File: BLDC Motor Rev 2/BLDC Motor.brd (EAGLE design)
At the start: 60.6 x 67 mm, 51 parts, among them IC1 7805TV, IC2 7815TV, Q1 TP2104, Q10 TP2104, Q12 IRFS, Q13 TP2104, Q15 IRFS, Q16 TP2104, Q18 IRFS, Q3 IRFS, Q4 TP2104, Q6 IRFS, Q7 TP2104, Q9 IRFS, U1 ATMEGA328P_TQFP, Y1 16M

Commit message: Updated BLDC schematic
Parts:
- added R15: 100k, SparkFun:0805
- added R16: 20k, SparkFun:0805
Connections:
- removed net N$12: U1.22
- new net BATTLEVEL: R15.1, R16.2, U1.22
- net BATTPOS: now also R15.2
- net GND: now also R16.1
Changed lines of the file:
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@@
 </element>
 <element name="Y1" library="SparkFun" package="HC49US" value="16M" x="12.7" y="14.605" rot="R180"/>
+<element name="R15" library="SparkFun" package="0805" value="100k" x="-1.905" y="1.905"/>
+<element name="R16" library="SparkFun" package="0805" value="20k" x="-4.826" y="1.905"/>
 </elements>
 <signals>
@@
 <wire x1="14.6575" y1="34.925" x2="14.6575" y2="41.54" width="0.508" layer="1"/>
 <wire x1="14.6575" y1="41.54" x2="11.7475" y2="44.45" width="0.508" layer="1"/>
-<wire x1="14.6575" y1="41.54" x2="17.515" y2="39.37" width="0" layer="19" extent="1-1"/>
-<wire x1="3.4925" y1="24.892" x2="13.405" y2="24.2" width="0" layer="19" extent="1-1"/>
+<contactref element="R16" pad="1"/>
+<wire x1="37.5725" y1="34.29" x2="39.4225" y2="40.005" width="0" layer="19" extent="1-1"/>
+<wire x1="31.4325" y1="24.4475" x2="33.3375" y2="27.94" width="0" layer="19" extent="1-1"/>
+<wire x1="-5.726" y1="1.905" x2="2.8194" y2="2.1463" width="0" layer="19" extent="1-1"/>
+<wire x1="13.405" y1="24.2" x2="3.4925" y2="24.892" width="0" layer="19" extent="1-1"/>
+<wire x1="17.515" y1="39.37" x2="14.6575" y2="41.54" width="0" layer="19" extent="1-1"/>
 </signal>
 <signal name="N$1">
@@
 <contactref element="U1" pad="28"/>
 </signal>
-<signal name="N$12">
-<contactref element="U1" pad="22"/>
-</signal>
 <signal name="N$15">
 <contactref element="U1" pad="32"/>
@@
 <wire x1="40.005" y1="65.405" x2="4.1275" y2="65.405" width="1.27" layer="16"/>
 <wire x1="4.1275" y1="65.405" x2="4.1275" y2="62.865" width="1.27" layer="16"/>
+<contactref element="R15" pad="2"/>
+<wire x1="-1.005" y1="1.905" x2="40.0325" y2="13.6525" width="0" layer="19" extent="1-16"/>
 </signal>
 <signal name="15V">
@@
 </polygon>
 </signal>
+<signal name="BATTLEVEL">
+<contactref element="R15" pad="1"/>
+<contactref element="R16" pad="2"/>
+<contactref element="U1" pad="22"/>
+<wire x1="-2.805" y1="1.905" x2="13.405" y2="31.5976" width="0" layer="19" extent="1-1"/>
+<wire x1="-3.926" y1="1.905" x2="-2.805" y2="1.905" width="0" layer="19" extent="1-1"/>
+</signal>
 </signals>

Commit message: Updating board
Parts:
- removed JP4: STAND-OFF, SparkFun:STAND-OFF
- added JP1: STAND-OFF, SparkFun:STAND-OFF
- R16: value 20k -> 22k
- moved JP2 57.6 mm to (79.4, 3.17)
- moved R15 43.9 mm to (16.8, 41.6)
- moved R16 43.0 mm to (16.8, 39.1), turned to 180 degrees
- moved Q10 42.1 mm to (45.1, 18.4), turned to 0 degrees
- moved Q13 36.6 mm to (45.1, 11.7), turned to 0 degrees
- moved R12 35.1 mm to (32.1, 17.5), turned to 180 degrees
- moved R6 34.8 mm to (32.1, 20.6)
- moved Q11 31.9 mm to (37.5, 19.4)
- moved R9 31.6 mm to (32.1, 37.5), turned to 180 degrees
- moved Q16 31.1 mm to (45.1, 5.08), turned to 0 degrees
- moved R3 31.1 mm to (32.1, 40.6)
- moved R1 29.7 mm to (11.1, 4.76), turned to 0 degrees
- moved R7 28.8 mm to (32.1, 14.0)
- moved Q18 27.0 mm to (68.3, 37.8)
- moved Q3 27.0 mm to (68.3, 37.8)
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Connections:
- net MOSI: now also Q4.2, Q5.2, R10.2; no longer Q16.2, Q17.2, R14.2
- net PULSE2: now also Q16.2, Q17.2, R14.2; no longer Q4.2, Q5.2, R10.2
- net PULSE3: now also Q13.2, Q14.2, R13.2; no longer Q7.2, Q8.2, R11.2
- net PULSE5: now also Q7.2, Q8.2, R11.2; no longer Q13.2, Q14.2, R13.2
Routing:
- net BATTPOS: track 90.2 -> 209.3 mm
- net N$5: track 13.9 -> 109.4 mm
- net N$13: track 13.0 -> 92.0 mm
- net N$19: track 18.1 -> 87.5 mm, vias 0 -> 1
- net N$9: track 111.7 -> 44.1 mm
- net N$16: track 11.5 -> 74.2 mm
- net PHASEA: track 116.4 -> 69.0 mm
- net MOSI: track 19.0 -> 56.7 mm, vias 0 -> 3
- net N$25: track 7.51 -> 44.0 mm, vias 0 -> 1
- net VCC: track 140.9 -> 105.4 mm
- net PULSE3: track 16.2 -> 38.5 mm, vias 0 -> 2
- net PULSE5: track 11.3 -> 33.2 mm, vias 0 -> 2
- net PULSE4: track 16.8 -> 36.9 mm, vias 0 -> 2
- net MISO: track 0.00 -> 19.9 mm, vias 0 -> 1
- net SCK: track 0.00 -> 19.3 mm, vias 0 -> 1
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- added copper zone on layer 16, net BATTPOS
- added copper zone on layer 16, net GND
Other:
- board size 60.6 x 67 mm -> 83.9 x 49.8 mm
- board text added: "Forrest Kaminski Thuan Pham Justin Morgan Team 12"

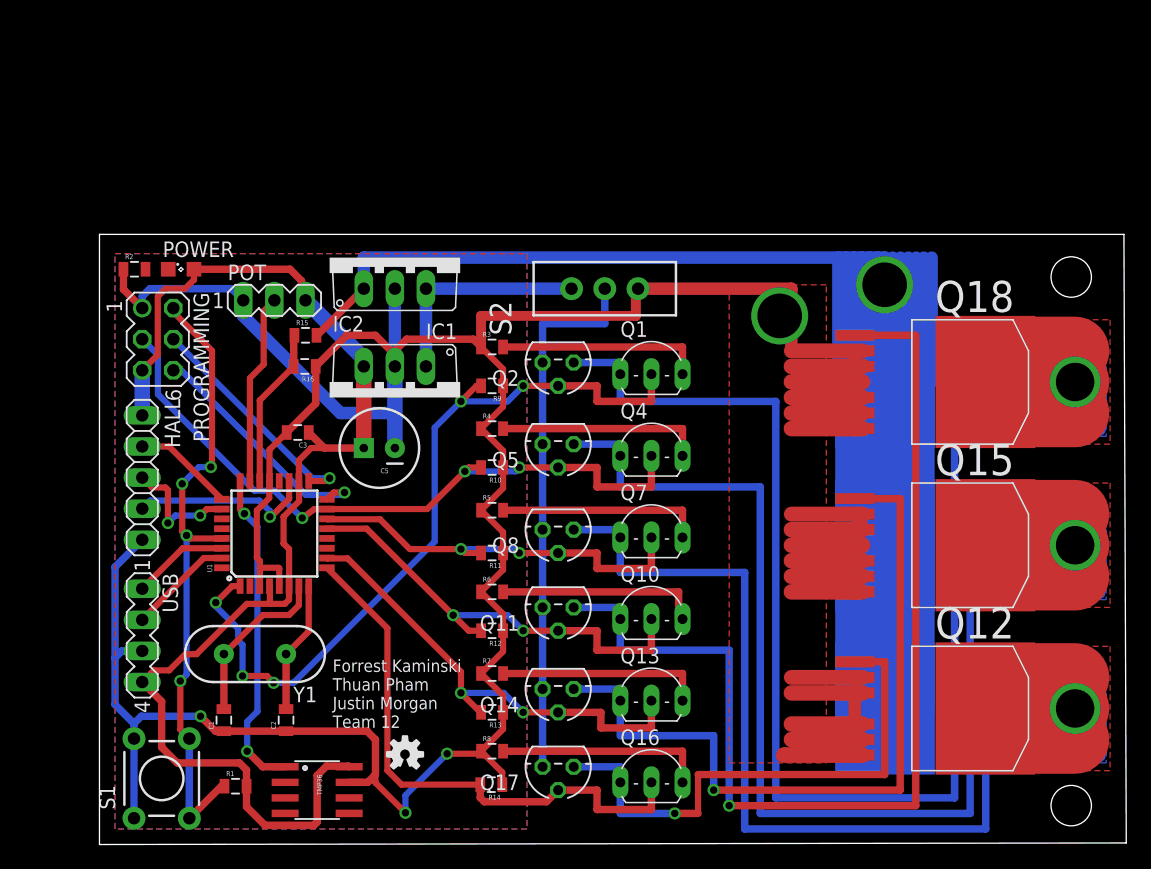
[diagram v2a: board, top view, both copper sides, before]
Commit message: Adding capacitors to the processor for better stability
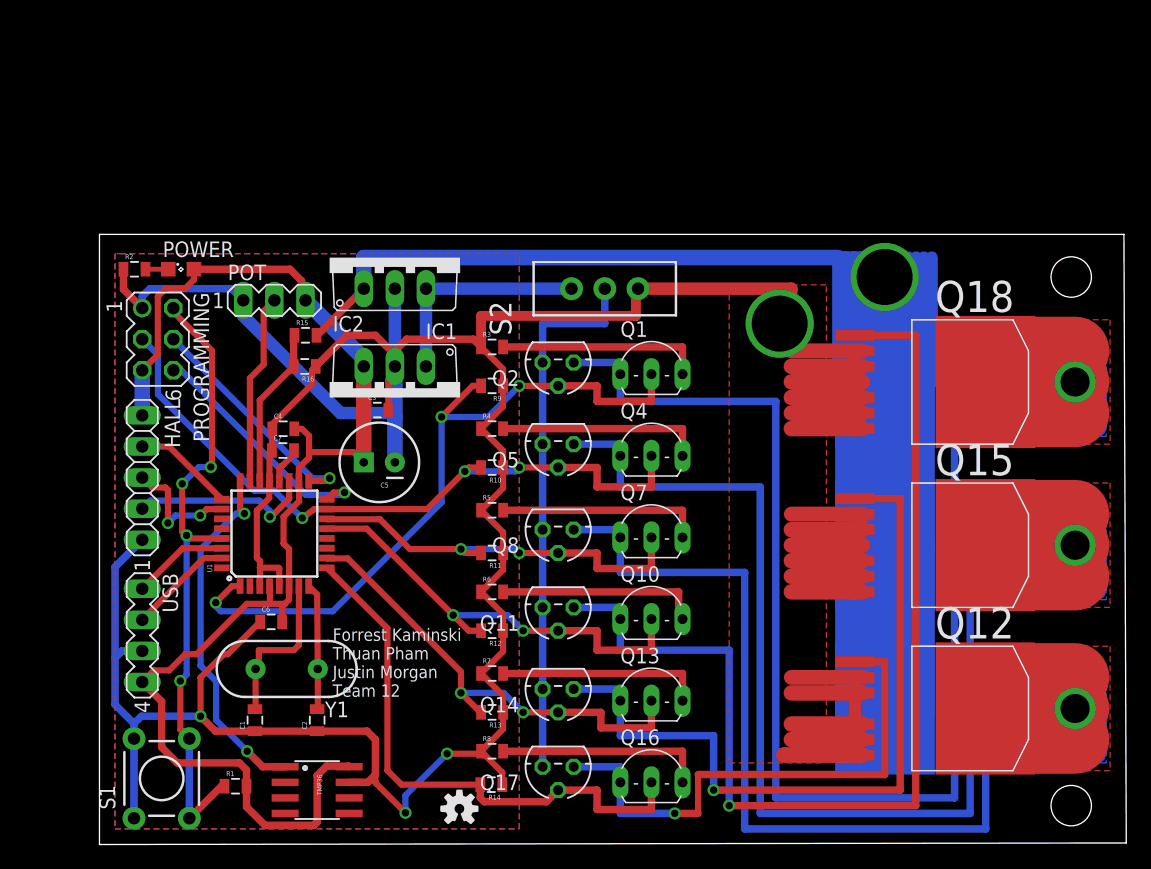
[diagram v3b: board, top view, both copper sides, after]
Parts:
- added C4, C6, C7: 22pf, SparkFun:0805
- moved C3 6.75 mm to (22.7, 35.5), turned to 0 degrees
- moved U$1 6.29 mm to (29.4, 2.92)
- moved Y1 2.86 mm to (15.3, 14.3)
- moved C2 2.54 mm to (17.8, 10.2)
- moved C1 2.54 mm to (12.7, 10.2)
- moved C5 1.17 mm to (22.9, 31.2)
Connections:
- new net N$7: C7.2, U1.20
- net GND: now also C4.1, C6.1, C7.1
- net VCC: now also C4.2, C6.2
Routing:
- net GND: track 355.0 -> 369.9 mm
- net VCC: track 105.4 -> 112.9 mm
- net PULSE1: track 64.2 -> 58.1 mm, vias 5 -> 3
- net N$7: track 0.00 -> 3.02 mm
- net N$6: track 27.0 -> 29.3 mm
- net N$3: track 0.00 -> 1.86 mm
- net BATTPOS: track 209.3 -> 210.6 mm
- net N$2: track 13.8 -> 13.2 mm

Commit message: Updated Gate driver on board, moved weekly reports to folder
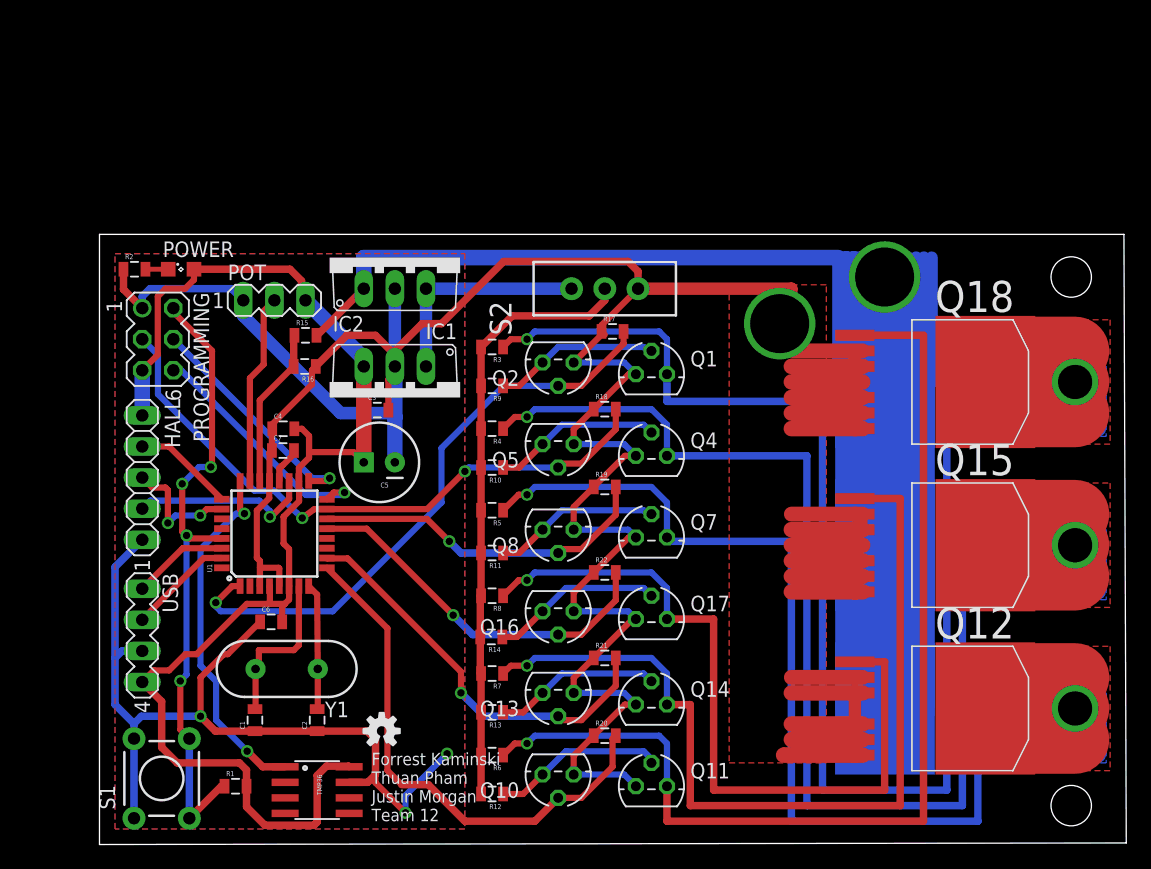
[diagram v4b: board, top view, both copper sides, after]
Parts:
- added R17, R18, R19, R20, R21, R22: 10k, SparkFun:0805
- Q1, Q10, Q13, Q16, Q4, Q7: value TP2104 -> (none); device adafruit:TO92-OVAL -> transistors:TO-92
- moved Q11 16.5 mm to (45.1, 4.76), turned to 0 degrees
- moved Q16 15.9 mm to (37.5, 19.1), turned to 180 degrees
- moved Q10 14.8 mm to (37.5, 5.71), turned to 180 degrees
- moved Q17 14.3 mm to (45.1, 18.4), turned to 0 degrees
- moved R6 13.3 mm to (32.1, 7.30), turned to 180 degrees
- moved R12 13.3 mm to (32.1, 4.13)
- moved R8 12.7 mm to (32.1, 20.3), turned to 180 degrees
- moved R14 12.1 mm to (32.0, 17.0)
- moved U$1 8.98 mm to (23.1, 9.27)
- moved Q14 7.73 mm to (45.1, 11.4), turned to 0 degrees
- moved Q13 7.65 mm to (37.5, 12.4), turned to 180 degrees
- turned R3 to 180 degrees
- turned R4 to 180 degrees
- turned R5 to 180 degrees
- turned R7 to 180 degrees
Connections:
- removed net N$10: Q4.3, R4.2
- removed net N$16: Q7.1, Q8.1, Q9.G
- removed net N$18: Q10.3, R6.2
- removed net N$23: Q13.1, Q14.1, Q15.G
- removed net N$24: Q16.3, R8.2
- removed net N$25: Q12.G, Q16.1, Q17.1
- new net N$11: Q4.2, Q5.3, R10.1
- new net N$12: R10.2, R11.2, R12.2, R13.2, R14.2, R3.2, R4.2, R5.2, R6.2, R7.2, R8.2, R9.2, S2.2
- new net N$26: Q12.G, Q17.3, R8.1
- new net N$27: Q16.3, Q17.2, R14.1
- new net N$28: Q14.3, Q15.G, R7.1
- new net N$8: Q1.2, Q2.3, R9.1
- net GND: now also Q1.1, Q10.1, Q11.1, Q13.1, Q14.1, Q16.1, Q17.1, Q2.1, Q4.1, Q5.1, Q7.1, Q8.1, R17.1, R18.1, R19.1, R20.1, R21.1, R22.1; no longer R10.1, R11.1, R12.1, R13.1, R14.1, R3.1, R4.1, R5.1, R6.1, R7.1, R8.1, R9.1
- net MOSI: now also R18.2; no longer Q4.2, R10.2
- net N$13: now also Q7.3, Q9.G, R5.1; no longer Q4.1, Q5.1, Q6.G
- net N$14: now also Q7.2, Q8.3, R11.1; no longer Q7.3, R5.2
- net N$19: now also Q11.3, R6.1; no longer Q10.1, Q11.1
- net N$22: now also Q14.2, R13.1; no longer R7.2
- net N$4: now also Q10.3, Q11.2, R12.1; no longer Q1.3, R3.2
- net N$5: now also Q1.3, R3.1; no longer Q1.1, Q2.1
- net N$9: now also Q4.3, Q6.G, R4.1; no longer Q11.3, Q14.3, Q17.3, Q2.3, Q5.3, Q8.3, S2.2
- net PULSE1: now also R17.2; no longer Q1.2, R9.2
- net PULSE2: now also Q10.2, R20.2; no longer Q16.2, Q17.2, R14.2
- net PULSE3: now also R21.2; no longer Q14.2, R13.2
- net PULSE4: now also Q16.2, R22.2; no longer Q10.2, Q11.2, R12.2
- net PULSE5: now also R19.2; no longer Q7.2, R11.2
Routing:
- net N$16: track 74.2 -> 0.00 mm
- net N$28: track 0.00 -> 73.1 mm, vias 0 -> 1
- net N$23: track 62.4 -> 0.00 mm, vias 1 -> 0
- net N$26: track 0.00 -> 61.9 mm, vias 0 -> 1
- net N$9: track 44.1 -> 99.2 mm, vias 0 -> 1
- net N$12: track 0.00 -> 49.3 mm
- net N$25: track 44.0 -> 0.00 mm, vias 1 -> 0
- net GND: track 369.9 -> 405.7 mm
- net N$24: track 17.2 -> 0.00 mm
- net N$18: track 16.9 -> 0.00 mm
- net N$10: track 16.9 -> 0.00 mm
- net N$27: track 0.00 -> 14.1 mm
- net N$11: track 0.00 -> 13.8 mm
- net N$8: track 0.00 -> 13.6 mm
- net N$13: track 92.0 -> 82.2 mm, vias 0 -> 1
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
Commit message: Final board design, added test arduino code
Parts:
- added JP3: (no value), SparkFun:1X07
- moved U$1 33.9 mm to (55.4, 19.4), turned to 90 degrees
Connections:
- net GND: now also JP3.1
- net MOSI: now also JP3.6
- net PULSE1: now also JP3.7
- net PULSE2: now also JP3.2
- net PULSE3: now also JP3.3
- net PULSE4: now also JP3.4
- net PULSE5: now also JP3.5
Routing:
- net GND: track 405.7 -> 456.2 mm
- net BATTPOS: track 210.6 -> 245.6 mm, vias 1 -> 2
- net PHASEC: track 69.2 -> 102.1 mm
- net PHASEB: track 69.0 -> 95.7 mm
- net PHASEA: track 69.0 -> 91.4 mm
- net PULSE2: track 43.2 -> 47.6 mm
- net PULSE3: track 33.5 -> 34.7 mm, vias 1 -> 0
- net MOSI: track 51.2 -> 51.8 mm, vias 2 -> 1
- net PULSE5: vias 1 -> 0
- net PULSE4: vias 1 -> 0
